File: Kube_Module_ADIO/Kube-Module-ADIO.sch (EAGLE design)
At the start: 13 parts, among them IC1 MCP23017SP

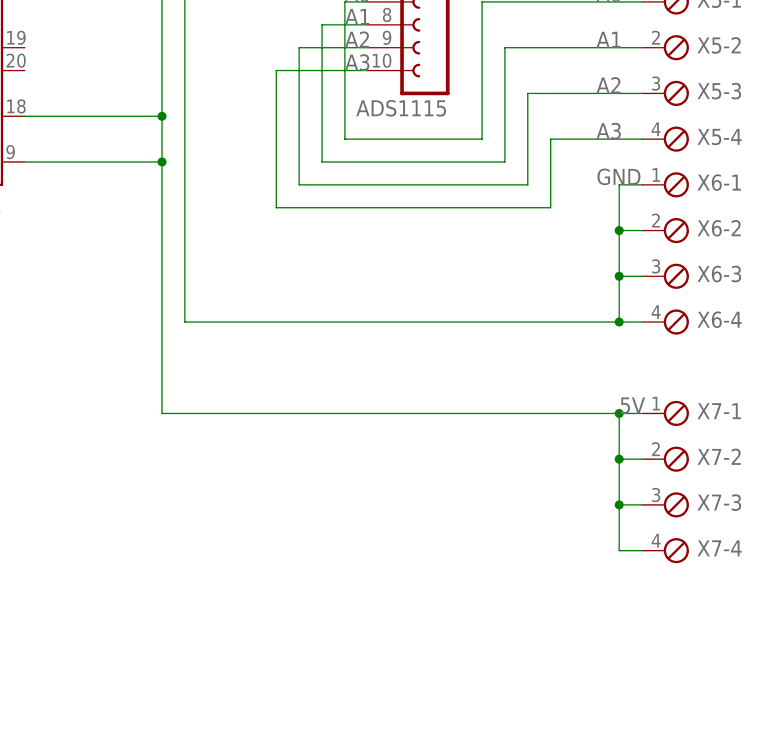
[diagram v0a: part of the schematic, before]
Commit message: Mods to ADIO to add add'l GND pins and space TBs better.
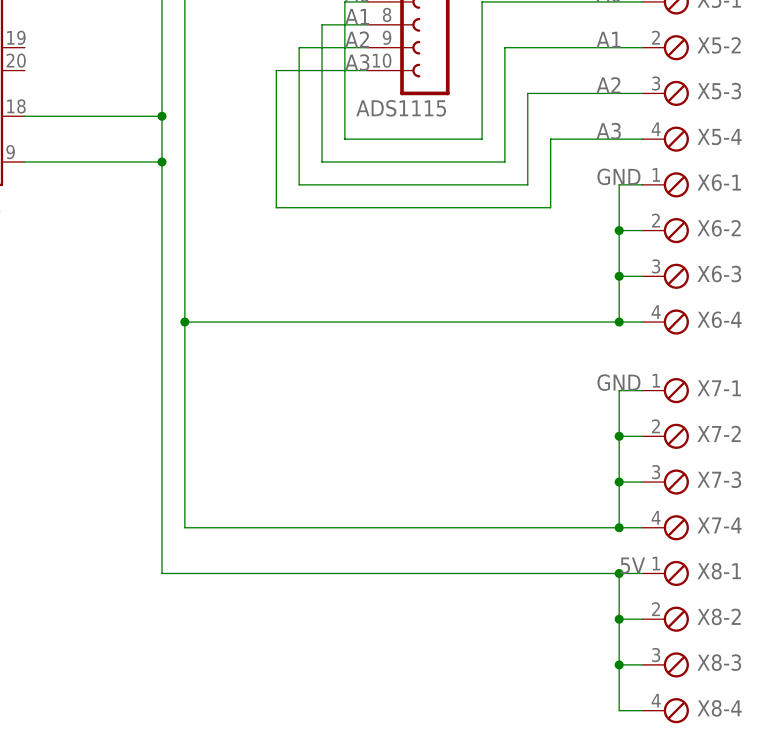
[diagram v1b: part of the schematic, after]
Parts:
- added X8: (no value), con-phoenix-254:MPT4
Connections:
- net 5V: now also X8-1.1, X8-2.1, X8-3.1, X8-4.1; no longer X7-1.1, X7-2.1, X7-3.1, X7-4.1
- net GND: now also X7-1.1, X7-2.1, X7-3.1, X7-4.1
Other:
- moved on the sheet: X7-1, X7-2, X7-3, X7-4
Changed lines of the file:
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@@
 <part name="X5" library="con-phoenix-254" library_urn="urn:adsk.eagle:library:172" deviceset="MPT4" device="" package3d_urn="urn:adsk.eagle:package:9326/1"/>
 <part name="X6" library="con-phoenix-254" library_urn="urn:adsk.eagle:library:172" deviceset="MPT4" device="" package3d_urn="urn:adsk.eagle:package:9326/1"/>
+<part name="X8" library="con-phoenix-254" library_urn="urn:adsk.eagle:library:172" deviceset="MPT4" device="" package3d_urn="urn:adsk.eagle:package:9326/1"/>
 <part name="X7" library="con-phoenix-254" library_urn="urn:adsk.eagle:library:172" deviceset="MPT4" device="" package3d_urn="urn:adsk.eagle:package:9326/1"/>
 </parts>
@@
 <attribute name="VALUE" x="125.984" y="-10.922" size="1.778" layer="96"/>
 </instance>
-<instance part="X7" gate="-1" x="127" y="-17.78" smashed="yes">
-<attribute name="NAME" x="130.556" y="-18.415" size="1.778" layer="95"/>
-</instance>
-<instance part="X7" gate="-2" x="127" y="-22.86" smashed="yes">
-<attribute name="NAME" x="130.556" y="-23.495" size="1.778" layer="95"/>
-</instance>
-<instance part="X7" gate="-3" x="127" y="-27.94" smashed="yes">
-<attribute name="NAME" x="130.556" y="-28.575" size="1.778" layer="95"/>
-</instance>
-<instance part="X7" gate="-4" x="127" y="-33.02" smashed="yes">
-<attribute name="NAME" x="130.556" y="-33.655" size="1.778" layer="95"/>
-<attribute name="VALUE" x="125.984" y="-36.322" size="1.778" layer="96"/>
+<instance part="X8" gate="-1" x="127" y="-35.56" smashed="yes">
+<attribute name="NAME" x="130.556" y="-36.195" size="1.778" layer="95"/>
+</instance>
+<instance part="X8" gate="-2" x="127" y="-40.64" smashed="yes">
+<attribute name="NAME" x="130.556" y="-41.275" size="1.778" layer="95"/>
+</instance>
+<instance part="X8" gate="-3" x="127" y="-45.72" smashed="yes">
+<attribute name="NAME" x="130.556" y="-46.355" size="1.778" layer="95"/>
+</instance>
+<instance part="X8" gate="-4" x="127" y="-50.8" smashed="yes">
+<attribute name="NAME" x="130.556" y="-51.435" size="1.778" layer="95"/>
+<attribute name="VALUE" x="125.984" y="-54.102" size="1.778" layer="96"/>
+</instance>
+<instance part="X7" gate="-1" x="127" y="-15.24" smashed="yes">
+<attribute name="NAME" x="130.556" y="-15.875" size="1.778" layer="95"/>
+</instance>
+<instance part="X7" gate="-2" x="127" y="-20.32" smashed="yes">
+<attribute name="NAME" x="130.556" y="-20.955" size="1.778" layer="95"/>
+</instance>
+<instance part="X7" gate="-3" x="127" y="-25.4" smashed="yes">
+<attribute name="NAME" x="130.556" y="-26.035" size="1.778" layer="95"/>
+</instance>
+<instance part="X7" gate="-4" x="127" y="-30.48" smashed="yes">
+<attribute name="NAME" x="130.556" y="-31.115" size="1.778" layer="95"/>
+<attribute name="VALUE" x="125.984" y="-33.782" size="1.778" layer="96"/>
 </instance>
 </instances>
@@
 <pinref part="AD0" gate="G$1" pin="1"/>
 <wire x1="35.56" y1="66.04" x2="30.48" y2="66.04" width="0.1524" layer="91"/>
-<wire x1="71.12" y1="10.16" x2="71.12" y2="-17.78" width="0.1524" layer="91"/>
+<wire x1="71.12" y1="10.16" x2="71.12" y2="-35.56" width="0.1524" layer="91"/>
 <junction x="71.12" y="10.16"/>
-<wire x1="124.46" y1="-17.78" x2="121.92" y2="-17.78" width="0.1524" layer="91"/>
-<label x="121.92" y="-17.78" size="1.778" layer="95"/>
+<wire x1="124.46" y1="-35.56" x2="121.92" y2="-35.56" width="0.1524" layer="91"/>
+<label x="121.92" y="-35.56" size="1.778" layer="95"/>
 <label x="91.44" y="43.18" size="1.778" layer="95"/>
-<wire x1="121.92" y1="-17.78" x2="71.12" y2="-17.78" width="0.1524" layer="91"/>
-<wire x1="124.46" y1="-22.86" x2="121.92" y2="-22.86" width="0.1524" layer="91"/>
-<wire x1="121.92" y1="-22.86" x2="121.92" y2="-17.78" width="0.1524" layer="91"/>
-<junction x="121.92" y="-17.78"/>
-<wire x1="121.92" y1="-22.86" x2="121.92" y2="-27.94" width="0.1524" layer="91"/>
-<junction x="121.92" y="-22.86"/>
-<wire x1="121.92" y1="-27.94" x2="124.46" y2="-27.94" width="0.1524" layer="91"/>
-<wire x1="124.46" y1="-33.02" x2="121.92" y2="-33.02" width="0.1524" layer="91"/>
-<wire x1="121.92" y1="-33.02" x2="121.92" y2="-27.94" width="0.1524" layer="91"/>
-<junction x="121.92" y="-27.94"/>
-<pinref part="X7" gate="-1" pin="1"/>
-<pinref part="X7" gate="-2" pin="1"/>
-<pinref part="X7" gate="-3" pin="1"/>
-<pinref part="X7" gate="-4" pin="1"/>
+<wire x1="121.92" y1="-35.56" x2="71.12" y2="-35.56" width="0.1524" layer="91"/>
+<wire x1="124.46" y1="-40.64" x2="121.92" y2="-40.64" width="0.1524" layer="91"/>
+<wire x1="121.92" y1="-40.64" x2="121.92" y2="-35.56" width="0.1524" layer="91"/>
+<junction x="121.92" y="-35.56"/>
+<wire x1="121.92" y1="-40.64" x2="121.92" y2="-45.72" width="0.1524" layer="91"/>
+<junction x="121.92" y="-40.64"/>
+<wire x1="121.92" y1="-45.72" x2="124.46" y2="-45.72" width="0.1524" layer="91"/>
+<wire x1="124.46" y1="-50.8" x2="121.92" y2="-50.8" width="0.1524" layer="91"/>
+<wire x1="121.92" y1="-50.8" x2="121.92" y2="-45.72" width="0.1524" layer="91"/>
+<junction x="121.92" y="-45.72"/>
+<pinref part="X8" gate="-1" pin="1"/>
+<pinref part="X8" gate="-2" pin="1"/>
+<pinref part="X8" gate="-3" pin="1"/>
+<pinref part="X8" gate="-4" pin="1"/>
 </segment>
 </net>
@@
 <net name="GND" class="0">
 <segment>
+<wire x1="124.46" y1="-15.24" x2="121.92" y2="-15.24" width="0.1524" layer="91"/>
+<wire x1="121.92" y1="-15.24" x2="121.92" y2="-20.32" width="0.1524" layer="91"/>
+<wire x1="121.92" y1="-20.32" x2="124.46" y2="-20.32" width="0.1524" layer="91"/>
+<wire x1="121.92" y1="-20.32" x2="121.92" y2="-25.4" width="0.1524" layer="91"/>
+<junction x="121.92" y="-20.32"/>
+<wire x1="121.92" y1="-25.4" x2="124.46" y2="-25.4" width="0.1524" layer="91"/>
+<wire x1="121.92" y1="-25.4" x2="121.92" y2="-30.48" width="0.1524" layer="91"/>
+<junction x="121.92" y="-25.4"/>
+<wire x1="121.92" y1="-30.48" x2="124.46" y2="-30.48" width="0.1524" layer="91"/>
+<wire x1="121.92" y1="-30.48" x2="73.66" y2="-30.48" width="0.1524" layer="91"/>
+<junction x="121.92" y="-30.48"/>
+<label x="119.38" y="-15.24" size="1.778" layer="95"/>
+<pinref part="X7" gate="-1" pin="1"/>
+<pinref part="X7" gate="-2" pin="1"/>
+<pinref part="X7" gate="-3" pin="1"/>
+<pinref part="X7" gate="-4" pin="1"/>
 <pinref part="ADS1115" gate="G$1" pin="5"/>
 <wire x1="93.98" y1="33.02" x2="83.82" y2="33.02" width="0.1524" layer="91"/>
@@
 <pinref part="X6" gate="-3" pin="1"/>
 <pinref part="X6" gate="-4" pin="1"/>
-</segment>
-</net>
+<wire x1="73.66" y1="-30.48" x2="73.66" y2="-7.62" width="0.1524" layer="91"/>
+<junction x="73.66" y="-7.62"/>
+</segment>
+</net>

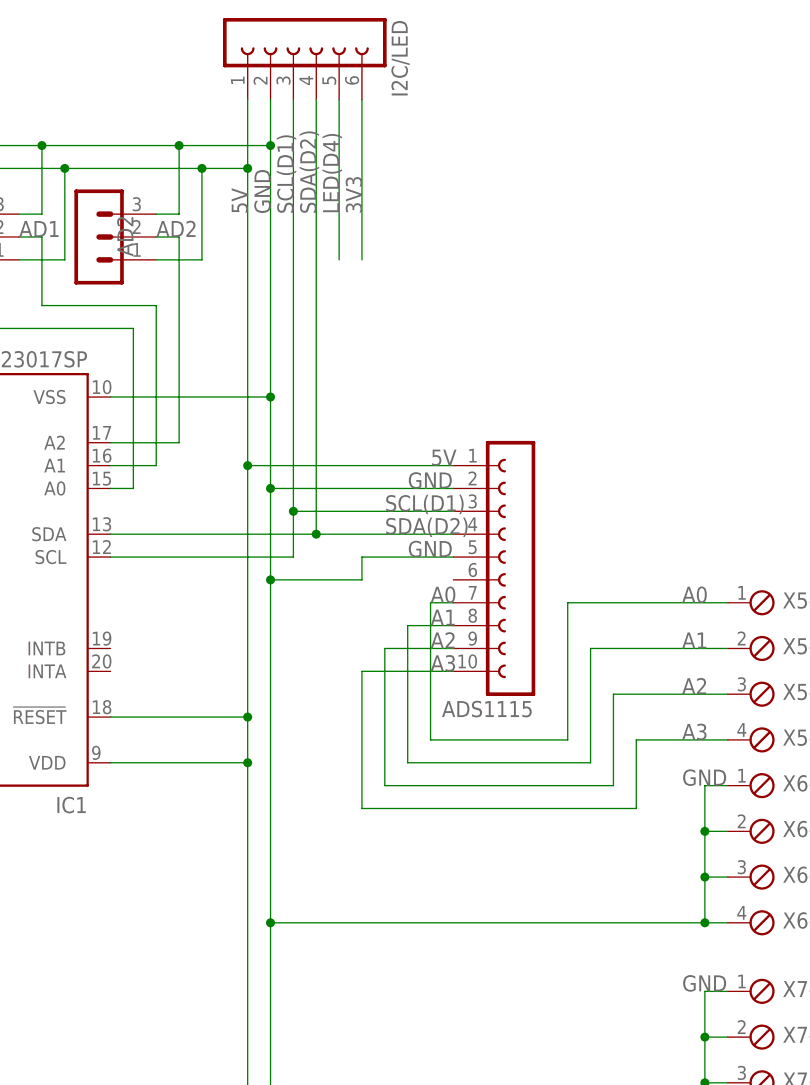
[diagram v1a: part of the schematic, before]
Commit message: Added ADS1115 addressing jumper
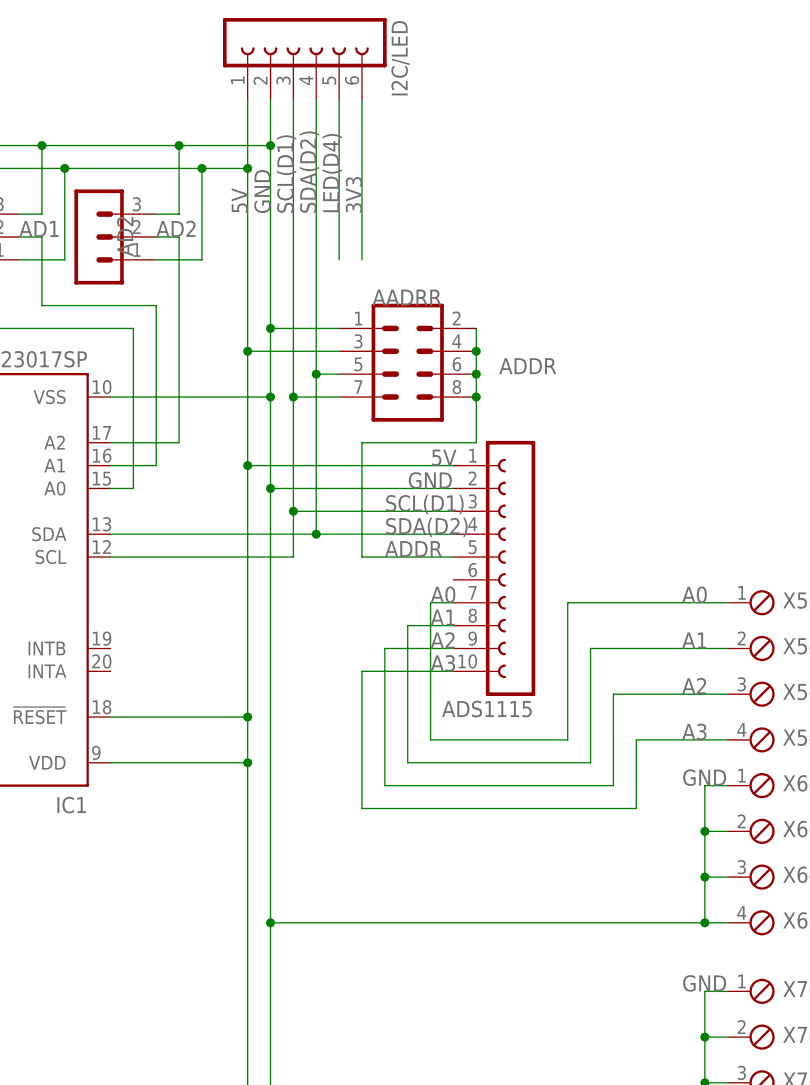
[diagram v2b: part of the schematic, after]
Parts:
- added AADRR: (no value), con-lstb:MA04-2
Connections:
- new net ADDR: AADRR.2, AADRR.4, AADRR.6, AADRR.8, ADS1115.5
- net 5V: now also AADRR.3
- net GND: now also AADRR.1; no longer ADS1115.5
- net SCL(D1): now also AADRR.7
- net SDA(D2): now also AADRR.5
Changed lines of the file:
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@@
 <?xml version="1.0" encoding="utf-8"?>
 <!DOCTYPE eagle SYSTEM "eagle.dtd">
-<eagle version="9.4.2">
+<eagle version="9.6.2">
 <drawing>
 <settings>
@@
 <layers>
 <layer number="1" name="Top" color="4" fill="1" visible="no" active="no"/>
+<layer number="2" name="Route2" color="1" fill="3" visible="no" active="no"/>
+<layer number="3" name="Route3" color="4" fill="3" visible="no" active="no"/>
+<layer number="4" name="Route4" color="1" fill="4" visible="no" active="no"/>
+<layer number="5" name="Route5" color="4" fill="4" visible="no" active="no"/>
+<layer number="6" name="Route6" color="1" fill="8" visible="no" active="no"/>
+<layer number="7" name="Route7" color="4" fill="8" visible="no" active="no"/>
+<layer number="8" name="Route8" color="1" fill="2" visible="no" active="no"/>
+<layer number="9" name="Route9" color="4" fill="2" visible="no" active="no"/>
+<layer number="10" name="Route10" color="1" fill="7" visible="no" active="no"/>
+<layer number="11" name="Route11" color="4" fill="7" visible="no" active="no"/>
+<layer number="12" name="Route12" color="1" fill="5" visible="no" active="no"/>
+<layer number="13" name="Route13" color="4" fill="5" visible="no" active="no"/>
+<layer number="14" name="Route14" color="1" fill="6" visible="no" active="no"/>
+<layer number="15" name="Route15" color="4" fill="6" visible="no" active="no"/>
 <layer number="16" name="Bottom" color="1" fill="1" visible="no" active="no"/>
 <layer number="17" name="Pads" color="2" fill="1" visible="no" active="no"/>
@@
 <part name="X8" library="con-phoenix-254" library_urn="urn:adsk.eagle:library:172" deviceset="MPT4" device="" package3d_urn="urn:adsk.eagle:package:9326/1"/>
 <part name="X7" library="con-phoenix-254" library_urn="urn:adsk.eagle:library:172" deviceset="MPT4" device="" package3d_urn="urn:adsk.eagle:package:9326/1"/>
+<part name="AADRR" library="con-lstb" library_urn="urn:adsk.eagle:library:162" deviceset="MA04-2" device="" package3d_urn="urn:adsk.eagle:package:8368/1"/>
 </parts>
 <sheets>
@@
 <attribute name="VALUE" x="125.984" y="-33.782" size="1.778" layer="96"/>
 </instance>
+<instance part="AADRR" gate="G$1" x="88.9" y="53.34" smashed="yes" rot="R180">
+<attribute name="VALUE" x="92.71" y="63.5" size="1.778" layer="96" rot="R180"/>
+<attribute name="NAME" x="92.71" y="62.738" size="1.778" layer="95" rot="R180"/>
+</instance>
 </instances>
 <busses>
@@
 <pinref part="I2C/LED" gate="G$1" pin="3"/>
 <label x="76.2" y="71.12" size="1.778" layer="95" rot="R90"/>
-<wire x1="76.2" y1="83.82" x2="76.2" y2="38.1" width="0.1524" layer="91"/>
+<wire x1="76.2" y1="83.82" x2="76.2" y2="50.8" width="0.1524" layer="91"/>
 <pinref part="IC1" gate="G$1" pin="SCL"/>
+<wire x1="76.2" y1="50.8" x2="76.2" y2="38.1" width="0.1524" layer="91"/>
 <wire x1="76.2" y1="38.1" x2="76.2" y2="33.02" width="0.1524" layer="91"/>
 <wire x1="76.2" y1="33.02" x2="55.88" y2="33.02" width="0.1524" layer="91"/>
@@
 <junction x="76.2" y="38.1"/>
 <label x="86.36" y="38.1" size="1.778" layer="95"/>
+<pinref part="AADRR" gate="G$1" pin="7"/>
+<wire x1="81.28" y1="50.8" x2="76.2" y2="50.8" width="0.1524" layer="91"/>
+<junction x="76.2" y="50.8"/>
 </segment>
 </net>
@@
 <pinref part="I2C/LED" gate="G$1" pin="4"/>
 <label x="78.74" y="71.12" size="1.778" layer="95" rot="R90"/>
-<wire x1="78.74" y1="83.82" x2="78.74" y2="35.56" width="0.1524" layer="91"/>
+<wire x1="78.74" y1="83.82" x2="78.74" y2="53.34" width="0.1524" layer="91"/>
 <pinref part="IC1" gate="G$1" pin="SDA"/>
+<wire x1="78.74" y1="53.34" x2="78.74" y2="35.56" width="0.1524" layer="91"/>
 <wire x1="78.74" y1="35.56" x2="55.88" y2="35.56" width="0.1524" layer="91"/>
 <pinref part="ADS1115" gate="G$1" pin="4"/>
@@
 <junction x="78.74" y="35.56"/>
 <label x="86.36" y="35.56" size="1.778" layer="95"/>
+<pinref part="AADRR" gate="G$1" pin="5"/>
+<wire x1="81.28" y1="53.34" x2="78.74" y2="53.34" width="0.1524" layer="91"/>
+<junction x="78.74" y="53.34"/>
 </segment>
 </net>
@@
 <wire x1="71.12" y1="83.82" x2="71.12" y2="76.2" width="0.1524" layer="91"/>
 <pinref part="ADS1115" gate="G$1" pin="1"/>
-<wire x1="71.12" y1="76.2" x2="71.12" y2="43.18" width="0.1524" layer="91"/>
+<wire x1="71.12" y1="76.2" x2="71.12" y2="55.88" width="0.1524" layer="91"/>
+<wire x1="71.12" y1="55.88" x2="71.12" y2="43.18" width="0.1524" layer="91"/>
 <wire x1="71.12" y1="43.18" x2="93.98" y2="43.18" width="0.1524" layer="91"/>
 <wire x1="71.12" y1="43.18" x2="71.12" y2="15.24" width="0.1524" layer="91"/>
@@
 <pinref part="X8" gate="-3" pin="1"/>
 <pinref part="X8" gate="-4" pin="1"/>
+<pinref part="AADRR" gate="G$1" pin="3"/>
+<wire x1="81.28" y1="55.88" x2="71.12" y2="55.88" width="0.1524" layer="91"/>
+<junction x="71.12" y="55.88"/>
 </segment>
 </net>
@@
 <pinref part="X7" gate="-3" pin="1"/>
 <pinref part="X7" gate="-4" pin="1"/>
-<pinref part="ADS1115" gate="G$1" pin="5"/>
-<wire x1="93.98" y1="33.02" x2="83.82" y2="33.02" width="0.1524" layer="91"/>
-<label x="88.9" y="33.02" size="1.778" layer="95"/>
 <pinref part="I2C/LED" gate="G$1" pin="2"/>
 <label x="73.66" y="71.12" size="1.778" layer="95" rot="R90"/>
 <pinref part="ADS1115" gate="G$1" pin="2"/>
 <wire x1="73.66" y1="83.82" x2="73.66" y2="78.74" width="0.1524" layer="91"/>
-<wire x1="73.66" y1="78.74" x2="73.66" y2="50.8" width="0.1524" layer="91"/>
+<wire x1="73.66" y1="78.74" x2="73.66" y2="58.42" width="0.1524" layer="91"/>
+<wire x1="73.66" y1="58.42" x2="73.66" y2="50.8" width="0.1524" layer="91"/>
 <wire x1="73.66" y1="50.8" x2="73.66" y2="40.64" width="0.1524" layer="91"/>
 <wire x1="73.66" y1="40.64" x2="93.98" y2="40.64" width="0.1524" layer="91"/>
@@
 <wire x1="33.02" y1="71.12" x2="30.48" y2="71.12" width="0.1524" layer="91"/>
 <junction x="73.66" y="40.64"/>
-<wire x1="73.66" y1="40.64" x2="73.66" y2="30.48" width="0.1524" layer="91"/>
-<wire x1="73.66" y1="30.48" x2="73.66" y2="-7.62" width="0.1524" layer="91"/>
+<wire x1="73.66" y1="40.64" x2="73.66" y2="-7.62" width="0.1524" layer="91"/>
 <label x="88.9" y="40.64" size="1.778" layer="95"/>
 <wire x1="124.46" y1="7.62" x2="121.92" y2="7.62" width="0.1524" layer="91"/>
@@
 <junction x="121.92" y="-7.62"/>
 <label x="119.38" y="7.62" size="1.778" layer="95"/>
-<wire x1="83.82" y1="33.02" x2="83.82" y2="30.48" width="0.1524" layer="91"/>
-<wire x1="83.82" y1="30.48" x2="73.66" y2="30.48" width="0.1524" layer="91"/>
-<junction x="73.66" y="30.48"/>
 <pinref part="X6" gate="-1" pin="1"/>
 <pinref part="X6" gate="-2" pin="1"/>
@@
 <wire x1="73.66" y1="-30.48" x2="73.66" y2="-7.62" width="0.1524" layer="91"/>
 <junction x="73.66" y="-7.62"/>
-</segment>
-</net>
+<pinref part="AADRR" gate="G$1" pin="1"/>
+<wire x1="81.28" y1="58.42" x2="73.66" y2="58.42" width="0.1524" layer="91"/>
+<junction x="73.66" y="58.42"/>
+</segment>
+</net>
+<net name="ADDR" class="0">
+<segment>
+<pinref part="AADRR" gate="G$1" pin="2"/>
+<pinref part="AADRR" gate="G$1" pin="4"/>
+<wire x1="96.52" y1="58.42" x2="96.52" y2="55.88" width="0.1524" layer="91"/>
+<pinref part="AADRR" gate="G$1" pin="6"/>
+<wire x1="96.52" y1="55.88" x2="96.52" y2="53.34" width="0.1524" layer="91"/>
+<junction x="96.52" y="55.88"/>
+<pinref part="AADRR" gate="G$1" pin="8"/>
+<wire x1="96.52" y1="53.34" x2="96.52" y2="50.8" width="0.1524" layer="91"/>
+<junction x="96.52" y="53.34"/>
+<wire x1="96.52" y1="50.8" x2="96.52" y2="45.72" width="0.1524" layer="91"/>
+<junction x="96.52" y="50.8"/>
+<wire x1="96.52" y1="45.72" x2="83.82" y2="45.72" width="0.1524" layer="91"/>
+<wire x1="83.82" y1="45.72" x2="83.82" y2="33.02" width="0.1524" layer="91"/>
+<pinref part="ADS1115" gate="G$1" pin="5"/>
+<wire x1="83.82" y1="33.02" x2="93.98" y2="33.02" width="0.1524" layer="91"/>
+<label x="86.36" y="33.02" size="1.778" layer="95"/>
+<label x="99.06" y="53.34" size="1.778" layer="95"/>
+</segment>
+</net>
